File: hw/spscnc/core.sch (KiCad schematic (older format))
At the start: 55 parts, among them J11 Conn_01x04, J7 USB_B_Micro, Q11 BSP41, Q12 BSP42, U13 74HC595, U14 74HC595, U3 NCP1117ST33T3G, U4 ESP32-WROOM-32D, U8 FT232RL

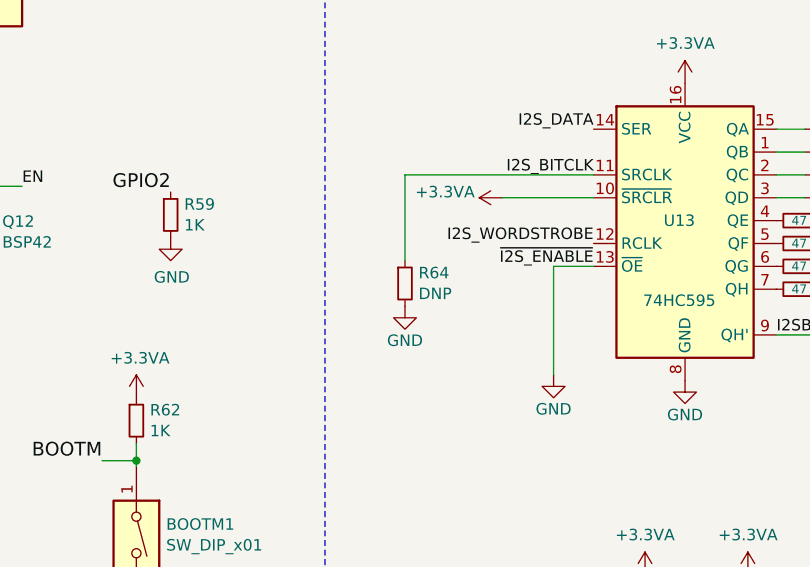
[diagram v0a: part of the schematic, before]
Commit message: Reported more defects
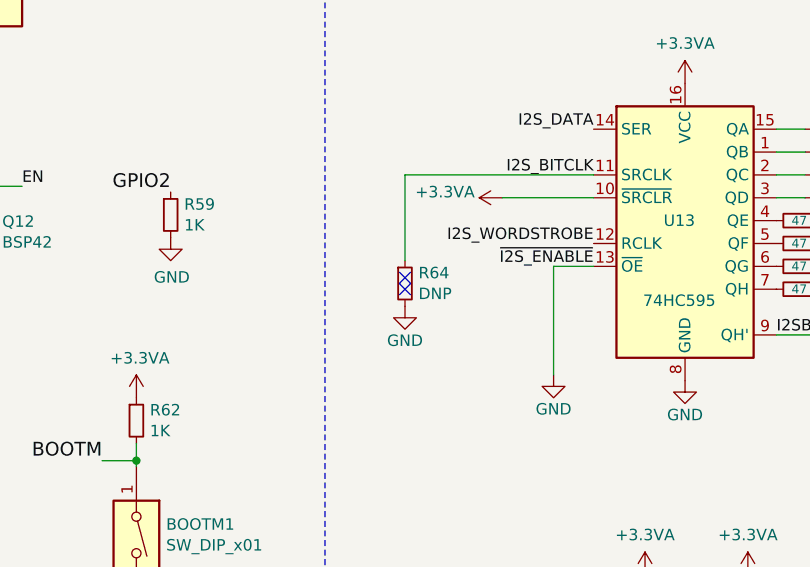
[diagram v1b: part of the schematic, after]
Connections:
- no-connect marks 19 -> 21
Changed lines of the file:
@@
 Text Notes 6425 8700 0    50   ~ 0
 Enable vacuum is glitching during start and reset.
+NoConn ~ 4775 5525
+NoConn ~ 4775 5575
 $EndSCHEMATC

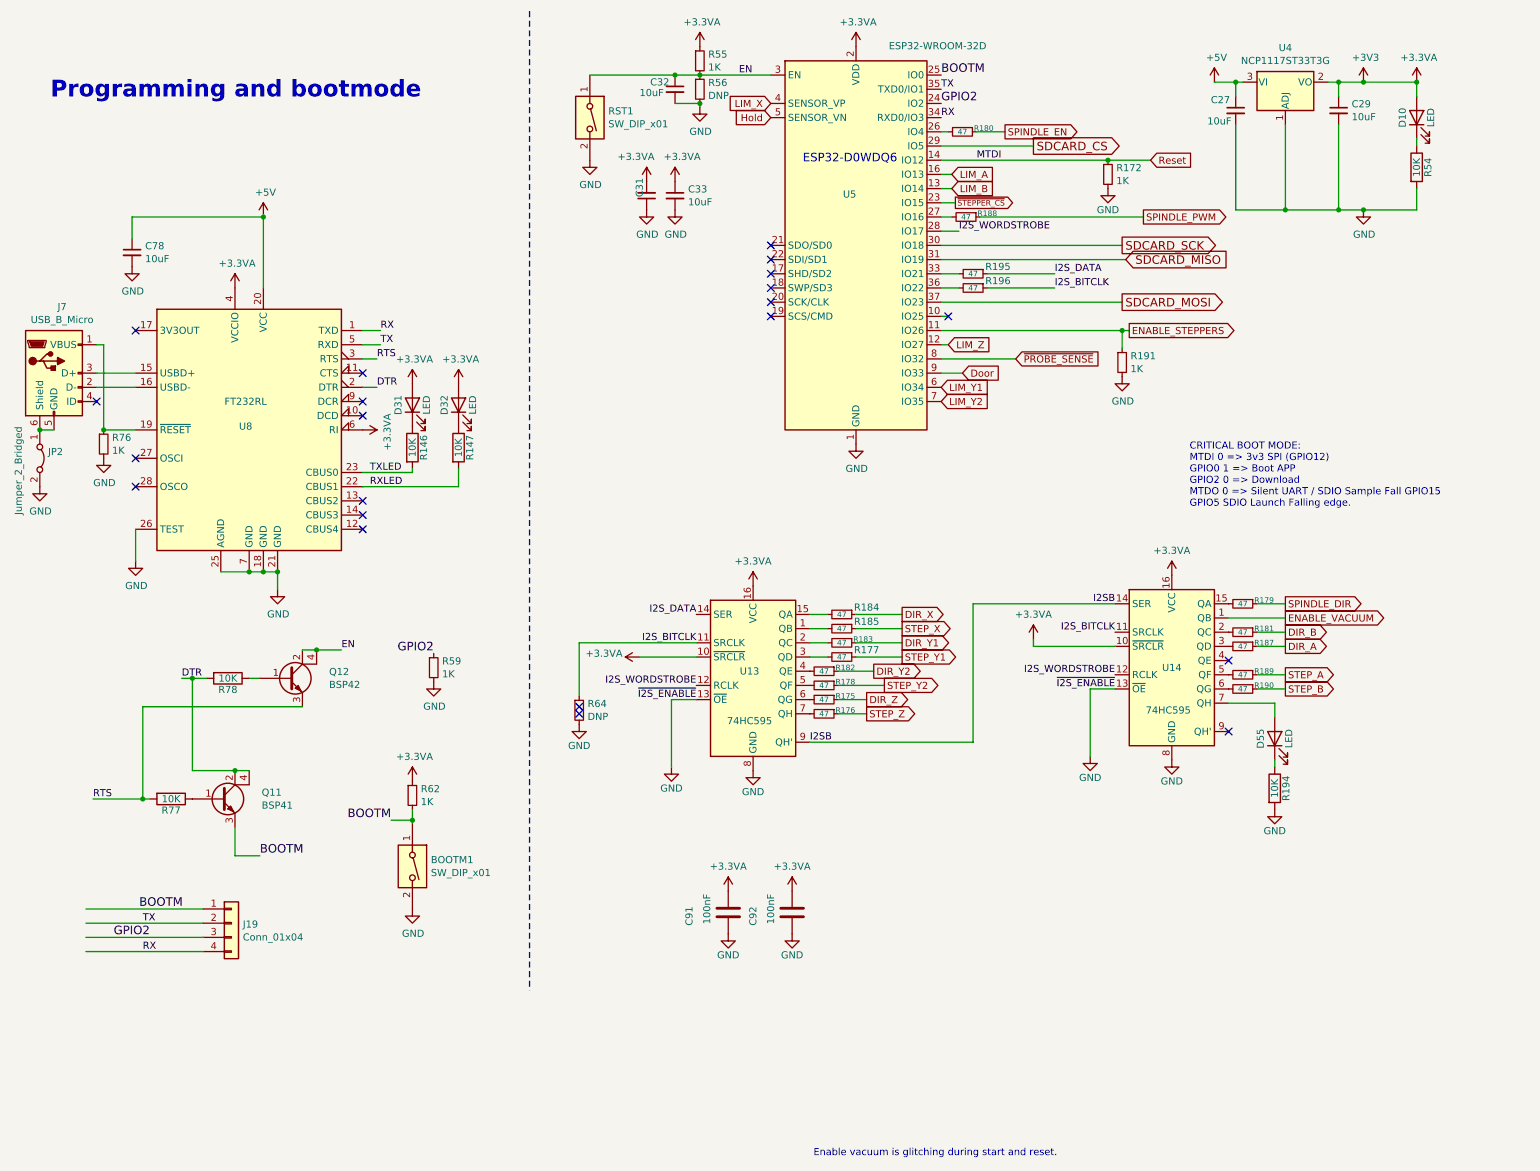
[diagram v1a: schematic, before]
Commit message: Revision 1.1.0 With only critical corrections. Pending some work on the relays as that part could be remade from scratch for flexibility.
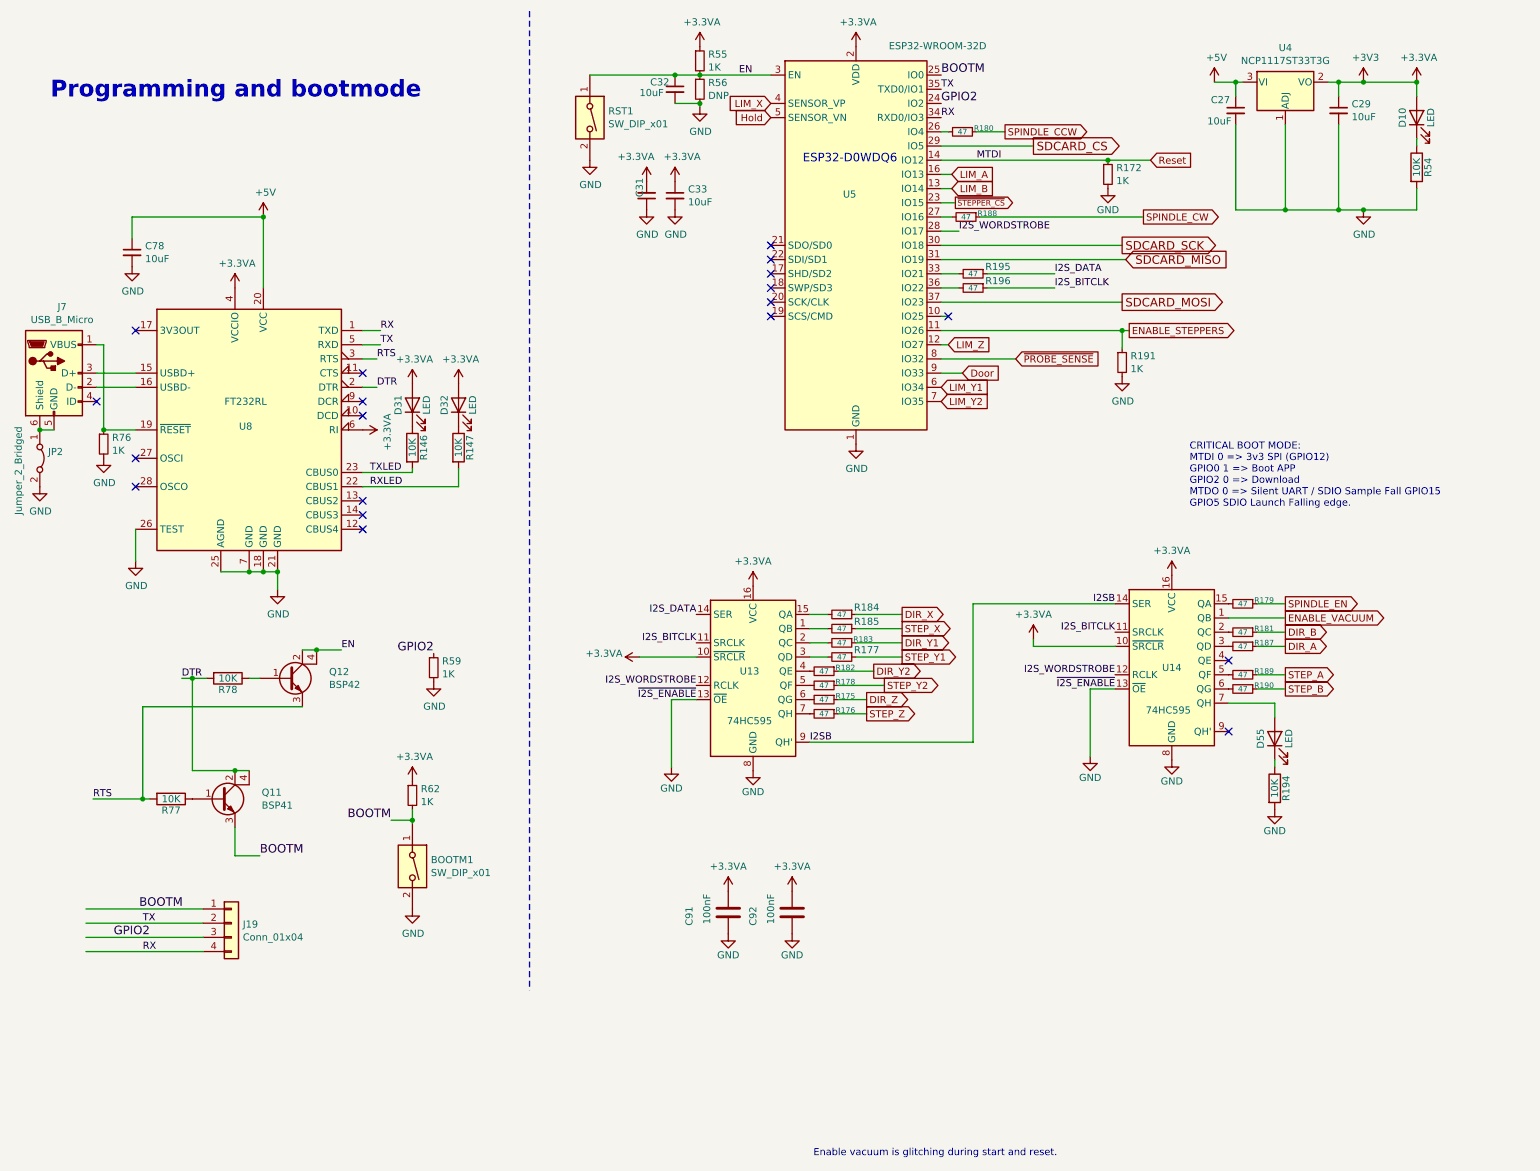
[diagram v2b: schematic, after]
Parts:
- removed R64: DNP, Resistor_SMD:R_0603_1608Metric, symbol Device:R_Small
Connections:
- net labels added: SPINDLE_CCW, SPINDLE_CW
- net labels removed: SPINDLE_DIR, SPINDLE_PWM
- wire segments 123 -> 121
- no-connect marks 21 -> 19
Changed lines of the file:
@@
 Sheet 6 17
 Title "Trinamic FluidNC CNC Controller"
-Date "2022-02-12"
-Rev "1.0.1"
+Date "2022-04-29"
+Rev "1.1.0"
 Comp ""
 Comment1 ""
@@
 Wire Wire Line
 	7450 2475 7325 2475
-Wire Wire Line
-	7375 2775 7325 2775
 Text GLabel 7325 3275 2    50   Input ~ 0
 LIM_Y1
@@
 Text Notes 9075 4125 0    50   ~ 0
 CRITICAL BOOT MODE:\nMTDI 0 => 3v3 SPI (GPIO12)\nGPIO0 1 => Boot APP\nGPIO2 0 => Download\nMTDO 0 => Silent UART / SDIO Sample Fall GPIO15\nGPIO5 SDIO Launch Falling edge.\n
-Text GLabel 7775 1475 2    50   Output ~ 0
+Text GLabel 9750 4800 2    50   Output ~ 0
 SPINDLE_EN
 Text GLabel 8650 2875 2    50   Output ~ 0
 ENABLE_STEPPERS
 Text GLabel 8750 2075 2    50   Output ~ 0
-SPINDLE_PWM
-Text GLabel 9750 4800 2    50   Output ~ 0
-SPINDLE_DIR
+SPINDLE_CW
 $Comp
 L Device:R_Small R?
@@
 	1    8600 3200
 	1    0    0    -1
-$EndComp
-$Comp
-L Device:R_Small R?
-U 1 1 62063E38
-P 9450 4800
-AR Path="/62063E38" Ref="R?"  Part="1"
-AR Path="/61C81F9D/62063E38" Ref="R179"  Part="1"
-F 0 "R179" V 9425 4950 39  0000 C CNN
-F 1 "47" V 9450 4800 39  0000 C CNN
-F 2 "Resistor_SMD:R_0805_2012Metric" V 9380 4800 50  0001 C CNN
-F 3 "~" H 9450 4800 50  0001 C CNN
-F 4 "C17714" H 9450 4800 50  0001 C CNN "jlcpcb"
-	1    9450 4800
-	0    1    1    0
 $EndComp
 $Comp
@@
 ~I2S_ENABLE
 Wire Wire Line
-	9750 4800 9550 4800
-Wire Wire Line
 	7600 2075 8750 2075
 Wire Wire Line
@@
 Text GLabel 9750 5300 2    50   Output ~ 0
 STEP_A
-Wire Wire Line
-	5600 5075 4775 5075
-Wire Wire Line
-	4775 5075 4775 5450
-$Comp
-L Device:R_Small R?
-U 1 1 62063E7E
-P 4775 5550
-AR Path="/61367F02/62063E7E" Ref="R?"  Part="1"
-AR Path="/5AD46BE5/619A452E/61B9A8A6/62063E7E" Ref="R?"  Part="1"
-AR Path="/61B9A8A6/62063E7E" Ref="R?"  Part="1"
-AR Path="/61C743E7/61B9A8A6/62063E7E" Ref="R?"  Part="1"
-AR Path="/61C81F9D/62063E7E" Ref="R64"  Part="1"
-F 0 "R64" H 4834 5596 50  0000 L CNN
-F 1 "DNP" H 4834 5505 50  0000 L CNN
-F 2 "Resistor_SMD:R_0603_1608Metric" H 4775 5550 50  0001 C CNN
-F 3 "~" H 4775 5550 50  0001 C CNN
-F 4 "DNP654" H 4775 5550 50  0001 C CNN "jlcpcb"
-	1    4775 5550
-	1    0    0    -1
-$EndComp
-$Comp
-L power:GND-power #PWR?
-U 1 1 62063E84
-P 4775 5650
-AR Path="/5AD46BE5/62063E84" Ref="#PWR?"  Part="1"
-AR Path="/5AD46BE5/619A452E/62063E84" Ref="#PWR?"  Part="1"
-AR Path="/62063E84" Ref="#PWR?"  Part="1"
-AR Path="/61B9A8A6/62063E84" Ref="#PWR?"  Part="1"
-AR Path="/61C743E7/61B9A8A6/62063E84" Ref="#PWR?"  Part="1"
-AR Path="/61C81F9D/62063E84" Ref="#PWR012"  Part="1"
-F 0 "#PWR012" H 4775 5400 50  0001 C CNN
-F 1 "GND" H 4775 5500 50  0000 C CNN
-F 2 "" H 4775 5650 50  0001 C CNN
-F 3 "" H 4775 5650 50  0001 C CNN
-	1    4775 5650
-	-1   0    0    -1
-$EndComp
 $Comp
 L power:GND-power #PWR?
@@
 	7550 5775 6400 5775
 NoConn ~ 9350 5700
-NoConn ~ 7375 2775
 $Comp
 L power:+3.3VA-power #PWR?
@@
 AR Path="/61B9A8A6/620826BE" Ref="#PWR?"  Part="1"
 AR Path="/61C743E7/61B9A8A6/620826BE" Ref="#PWR?"  Part="1"
-AR Path="/61C81F9D/620826BE" Ref="#PWR?"  Part="1"
+AR Path="/61C81F9D/620826BE" Ref="#PWR0175"  Part="1"
 AR Path="/620826BE" Ref="#PWR?"  Part="1"
-F 0 "#PWR?" H 7975 4900 50  0001 C CNN
+F 0 "#PWR0175" H 7975 4900 50  0001 C CNN
 F 1 "+3.3VA" H 7975 5225 50  0000 C CNN
 F 2 "" H 7975 5050 50  0001 C CNN
@@
 AR Path="/61B9A8A6/6208D205" Ref="#PWR?"  Part="1"
 AR Path="/61C743E7/61B9A8A6/6208D205" Ref="#PWR?"  Part="1"
-AR Path="/61C81F9D/6208D205" Ref="#PWR?"  Part="1"
+AR Path="/61C81F9D/6208D205" Ref="#PWR0198"  Part="1"
 AR Path="/6208D205" Ref="#PWR?"  Part="1"
-F 0 "#PWR?" H 5200 5025 50  0001 C CNN
+F 0 "#PWR0198" H 5200 5025 50  0001 C CNN
 F 1 "+3.3VA" V 5225 5425 50  0000 C CNN
 F 2 "" H 5200 5175 50  0001 C CNN
@@
 Text Notes 6425 8700 0    50   ~ 0
 Enable vacuum is glitching during start and reset.
-NoConn ~ 4775 5525
-NoConn ~ 4775 5575
+Wire Wire Line
+	7375 2775 7325 2775
+NoConn ~ 7375 2775
+Wire Wire Line
+	9750 4800 9550 4800
+$Comp
+L Device:R_Small R?
+U 1 1 62063E38
+P 9450 4800
+AR Path="/62063E38" Ref="R?"  Part="1"
+AR Path="/61C81F9D/62063E38" Ref="R179"  Part="1"
+F 0 "R179" V 9425 4950 39  0000 C CNN
+F 1 "47" V 9450 4800 39  0000 C CNN
+F 2 "Resistor_SMD:R_0805_2012Metric" V 9380 4800 50  0001 C CNN
+F 3 "~" H 9450 4800 50  0001 C CNN
+F 4 "C17714" H 9450 4800 50  0001 C CNN "jlcpcb"
+	1    9450 4800
+	0    1    1    0
+$EndComp
+Text GLabel 7775 1475 2    50   Output ~ 0
+SPINDLE_CCW
 $EndSCHEMATC
